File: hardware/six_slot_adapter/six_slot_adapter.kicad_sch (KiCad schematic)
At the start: 21 parts, among them J3 CART SLOT TOP ROW, J4 CART SLOT BOTTOM ROW, M2_1 Screw_Terminal_01x01, M2_2 Screw_Terminal_01x01, M2_3 Screw_Terminal_01x01, M2_4 Screw_Terminal_01x01, M2_5 Screw_Terminal_01x01, M2_6 Screw_Terminal_01x01, M2_7 Screw_Terminal_01x01, M2_8 Screw_Terminal_01x01, M2_9 Screw_Terminal_01x01

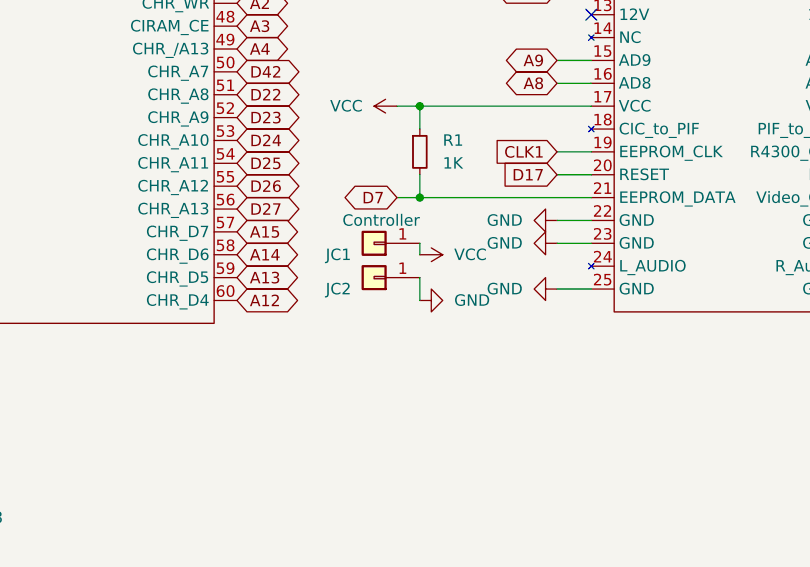
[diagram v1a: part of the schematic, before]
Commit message: Change N64 controller connector pitch to 2.54mm
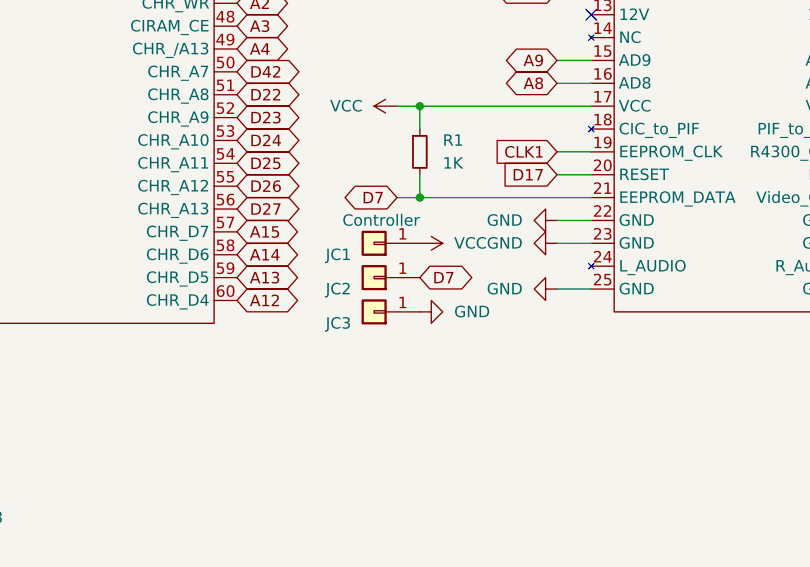
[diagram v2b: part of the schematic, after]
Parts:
- added JC2: Conn_01x01, symbol Connector_Generic:Conn_01x01
- renumbered JC2 to JC3
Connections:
- net D7: now also JC2.1 (Pin_1)
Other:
- moved on the sheet: JC3
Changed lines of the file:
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@@
   (title_block
     (title "SIX SLOT ADAPTER")
-    (date "2022-08-19")
-    (rev "V2")
+    (date "2022-10-17")
+    (rev "V3")
   )
   (junction (at 191.77 64.77) (diameter 0) (color 0 0 0 0)
@@
     (stroke (width 0) (type default) (color 0 0 0 0))
   )
-  (wire (pts (xy 220.98 156.21) (xy 220.98 157.48))
-    (stroke (width 0) (type default) (color 0 0 0 0))
-  )
   (wire (pts (xy 191.77 64.77) (xy 191.77 69.85))
     (stroke (width 0) (type default) (color 0 0 0 0))
@@
     (stroke (width 0) (type default) (color 0 0 0 0))
   )
-  (wire (pts (xy 220.98 160.02) (xy 220.98 162.56))
-    (stroke (width 0) (type default) (color 0 0 0 0))
-  )
   (wire (pts (xy 25.4 154.94) (xy 30.48 154.94))
     (stroke (width 0) (type default) (color 0 0 0 0))
@@
     )
   )
+  (global_label "D7" (shape bidirectional) (at 220.98 160.02 0) (fields_autoplaced)
+    (effects (font (size 1.27 1.27)) (justify left))
+    (property "Intersheet References" "${INTERSHEET_REFS}" (id 0) (at 225.8726 160.0994 0)
+      (effects (font (size 1.27 1.27)) (justify left) hide)
+    )
+  )
   (global_label "D48" (shape input) (at 77.47 114.3 0) (fields_autoplaced)
     (effects (font (size 1.27 1.27)) (justify left))
@@
     (pin "9")
   )
-  (symbol (lib_id "power:GND") (at 220.98 162.56 90) (unit 1)
+  (symbol (lib_id "power:GND") (at 220.98 163.83 90) (unit 1)
     (in_bom yes) (on_board yes) (fields_autoplaced)
-    (property "Reference" "#PWR0102" (id 0) (at 227.33 162.56 0)
+    (property "Reference" "#PWR0102" (id 0) (at 227.33 163.83 0)
       (effects (font (size 1.27 1.27)) hide)
     )
-    (property "Value" "GND" (id 1) (at 224.79 162.5599 90)
+    (property "Value" "GND" (id 1) (at 224.79 163.8299 90)
       (effects (font (size 1.27 1.27)) (justify right))
     )
-    (property "Footprint" "" (id 2) (at 220.98 162.56 0)
+    (property "Footprint" "" (id 2) (at 220.98 163.83 0)
       (effects (font (size 1.27 1.27)) hide)
     )
-    (property "Datasheet" "" (id 3) (at 220.98 162.56 0)
+    (property "Datasheet" "" (id 3) (at 220.98 163.83 0)
       (effects (font (size 1.27 1.27)) hide)
     )
@@
     (pin "9")
   )
-  (symbol (lib_id "power:VCC") (at 220.98 157.48 270) (unit 1)
+  (symbol (lib_id "power:VCC") (at 220.98 156.21 270) (unit 1)
     (in_bom yes) (on_board yes) (fields_autoplaced)
-    (property "Reference" "#PWR0101" (id 0) (at 217.17 157.48 0)
+    (property "Reference" "#PWR0101" (id 0) (at 217.17 156.21 0)
       (effects (font (size 1.27 1.27)) hide)
     )
-    (property "Value" "VCC" (id 1) (at 224.79 157.4799 90)
+    (property "Value" "VCC" (id 1) (at 224.79 156.2099 90)
       (effects (font (size 1.27 1.27)) (justify left))
     )
-    (property "Footprint" "" (id 2) (at 220.98 157.48 0)
+    (property "Footprint" "" (id 2) (at 220.98 156.21 0)
       (effects (font (size 1.27 1.27)) hide)
     )
-    (property "Datasheet" "" (id 3) (at 220.98 157.48 0)
+    (property "Datasheet" "" (id 3) (at 220.98 156.21 0)
       (effects (font (size 1.27 1.27)) hide)
     )
@@
     (pin "1")
   )
-  (symbol (lib_id "Connector_Generic:Conn_01x01") (at 215.9 160.02 180) (unit 1)
+  (symbol (lib_id "Connector_Generic:Conn_01x01") (at 215.9 163.83 180) (unit 1)
     (in_bom yes) (on_board yes)
-    (property "Reference" "JC2" (id 0) (at 213.36 161.2901 0)
+    (property "Reference" "JC3" (id 0) (at 213.36 165.1001 0)
       (effects (font (size 1.27 1.27)) (justify left))
     )
-    (property "Value" "Conn_01x01" (id 1) (at 220.98 163.83 0)
+    (property "Value" "Conn_01x01" (id 1) (at 220.98 167.64 0)
       (effects (font (size 1.27 1.27)) (justify left) hide)
     )
-    (property "Footprint" "" (id 2) (at 215.9 160.02 0)
+    (property "Footprint" "" (id 2) (at 215.9 163.83 0)
       (effects (font (size 1.27 1.27)) hide)
     )
-    (property "Datasheet" "~" (id 3) (at 215.9 160.02 0)
+    (property "Datasheet" "~" (id 3) (at 215.9 163.83 0)
       (effects (font (size 1.27 1.27)) hide)
     )
@@
     (pin "1")
   )
+  (symbol (lib_id "Connector_Generic:Conn_01x01") (at 215.9 160.02 180) (unit 1)
+    (in_bom yes) (on_board yes)
+    (property "Reference" "JC2" (id 0) (at 213.36 161.2901 0)
+      (effects (font (size 1.27 1.27)) (justify left))
+    )
+    (property "Value" "Conn_01x01" (id 1) (at 220.98 163.83 0)
+      (effects (font (size 1.27 1.27)) (justify left) hide)
+    )
+    (property "Footprint" "" (id 2) (at 215.9 160.02 0)
+      (effects (font (size 1.27 1.27)) hide)
+    )
+    (property "Datasheet" "~" (id 3) (at 215.9 160.02 0)
+      (effects (font (size 1.27 1.27)) hide)
+    )
+    (pin "1")
+  )
   (symbol (lib_id "!OSCR:N64_Slot") (at 252.73 129.54 0) (unit 1)
     (in_bom yes) (on_board yes)
@@
       (reference "JC1") (unit 1) (value "Controller") (footprint "")
     )
-    (path "/8208d08c-ec96-49c2-b035-10a14a4d6fdb"
+    (path "/9e004409-4f4f-4708-b6a7-05db86fc2109"
       (reference "JC2") (unit 1) (value "Conn_01x01") (footprint "")
     )
+    (path "/8208d08c-ec96-49c2-b035-10a14a4d6fdb"
+      (reference "JC3") (unit 1) (value "Conn_01x01") (footprint "")
+    )
     (path "/44ef40ed-afb0-4633-b46f-d94ccda95e42"

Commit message: Minor fixes/changes to six-slot adapter and git repository
* Add JLCPCB order ID text to Six-Slot Adapter; you can select "specify location" for order number location when ordering from JLCPCB. It is placed so the SNES slot covers it. (PCB revision not incremented because it is only a minor change to the silkscreen.)
* Added relative path for footprint and symbol libs to six-slot adapter project files.
* Added footprint details/links to schematic symbols.
* Added .gitignore and included most of the files that should remain local-only.
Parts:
- FC1: footprint (none) -> !OSCR:FC_Slot
- JC1, JC2, JC3: footprint (none) -> Connector_PinHeader_2.54mm:PinHeader_1x01_P2.54mm_Vertical
- JCIC1: footprint (none) -> Connector_PinHeader_2.54mm:PinHeader_1x08_P2.54mm_Vertical
- M2_1, M2_2, M2_3, M2_4, M2_5, M2_6, M2_7, M2_8, M2_9: footprint (none) -> MountingHole:MountingHole_2.2mm_M2_ISO7380_Pad
- MD1: footprint (none) -> !OSCR:MD_Slot
- N64: footprint (none) -> !OSCR:N64 Slot
- NES1: footprint (none) -> !OSCR:NES_Slot
- R1: footprint (none) -> Resistor_THT:R_Axial_DIN0207_L6.3mm_D2.5mm_P10.16mm_Horizontal
- SMS1: footprint (none) -> !OSCR:SMS_Slot
- SNES1: footprint (none) -> !OSCR:SNES Slot

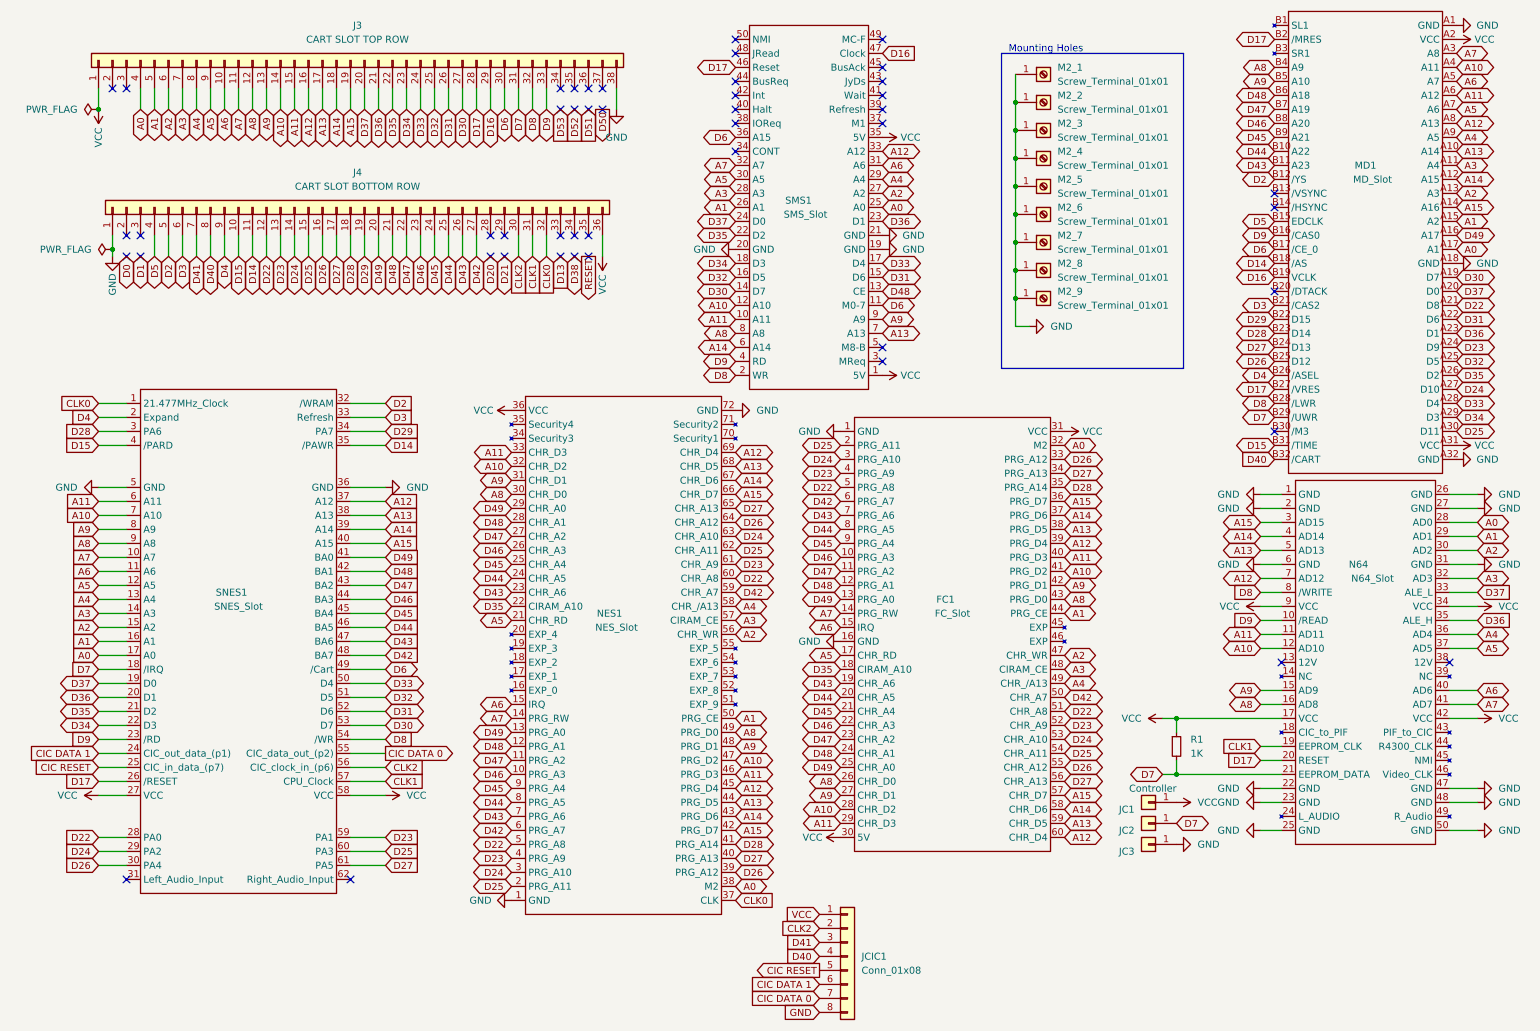
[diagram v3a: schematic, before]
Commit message: Add 12V rail for N64 + silkscreen updates
Add a 12V rail for the N64 slot. This is not currently implemented, but as the six-slot adapter is the hardest of the 2 boards to upgrade having it now will save some effort for anyone wanting it in the future. It also makes it easier to externally supply 12V by attaching clips to the 12V and GND header pins.

Also improved the silkscreen a bit to match the main PCB.
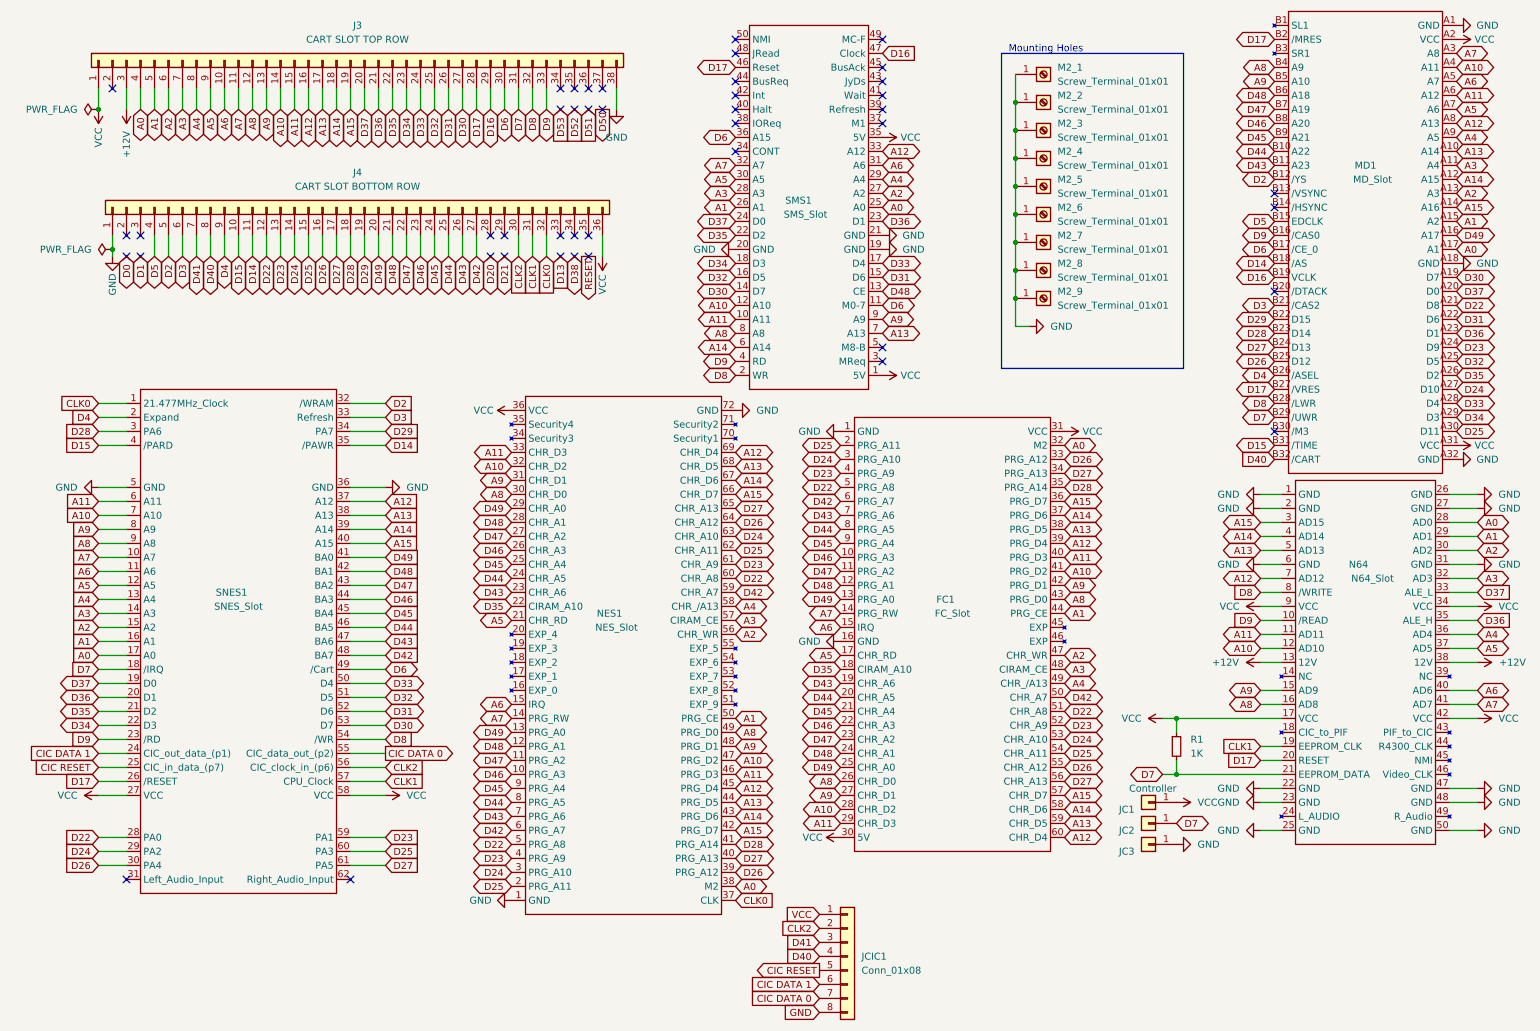
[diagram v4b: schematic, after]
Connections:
- net +12V: now reaches J3.3 (Pin_3)
- net +12V: now also N64.13 (12V), N64.38 (12V)
- no-connect marks 47 -> 44
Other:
- title: SIX SLOT ADAPTER -> SIX-SLOT ADAPTER
